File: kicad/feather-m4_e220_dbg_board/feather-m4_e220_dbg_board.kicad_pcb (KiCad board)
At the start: 2 copper layers, 61 x 60.5 mm, 10 parts

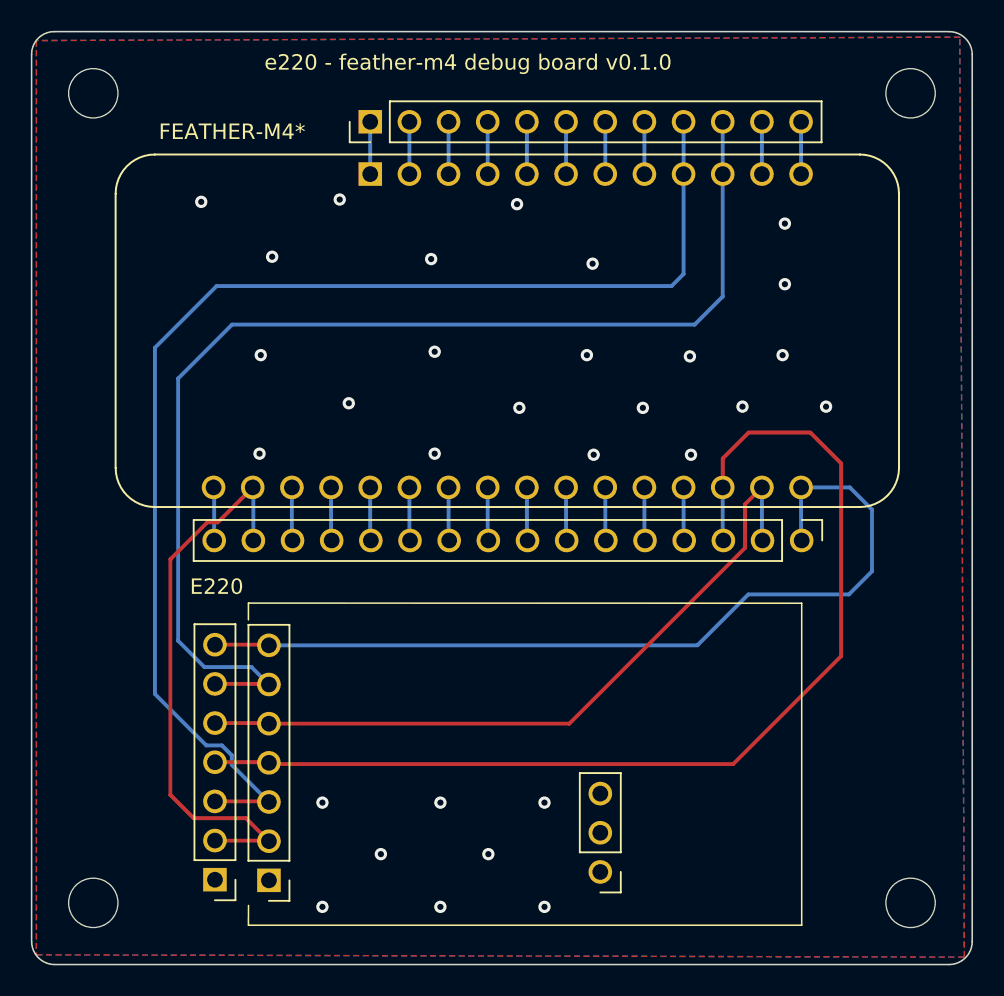
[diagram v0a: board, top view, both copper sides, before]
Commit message: Changed to place through holes for remaining E220 (as Pin8-9)
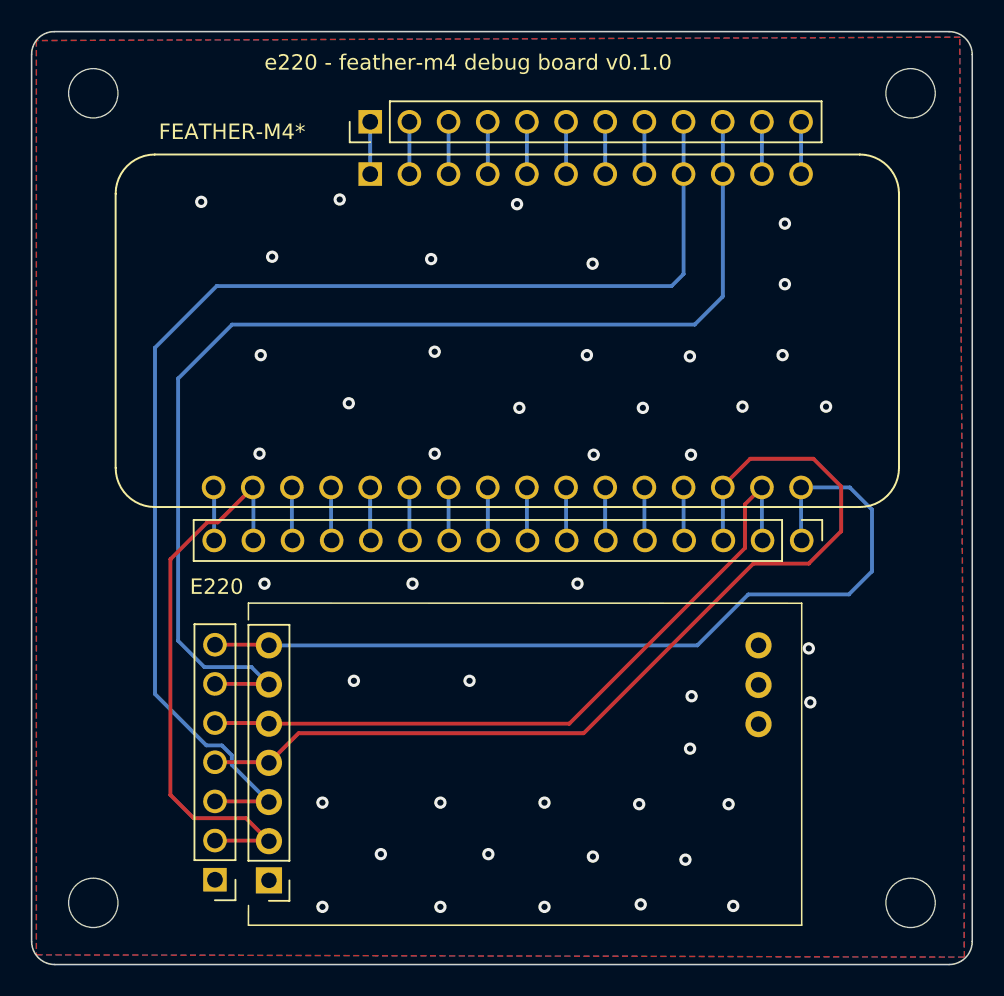
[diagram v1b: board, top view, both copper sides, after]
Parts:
- removed the REF** at (155.9, 124.0)
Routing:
- net Net-(U1-D0): track 70.6 -> 62.4 mm
- net GND: vias 30 -> 45

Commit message: add pin numbers of E220 to PCB
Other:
- board text added: "M0 01 M1 02 RXD 03 TXD 04 AUX 05 VCC 06 GND 07"
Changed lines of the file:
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@@
   (gr_arc (start 120.5 130) (mid 119.43934 129.56066) (end 119 128.5)
     (stroke (width 0.1) (type default)) (layer "Edge.Cuts"))
+  (gr_text "M0 01\nM1 02\nRXD 03\nTXD 04\nAUX 05\nVCC 06\nGND 07" (at 129.5 125.7) (layer "F.SilkS")
+    (effects (font (size 1.59 0.9) (thickness 0.15)) (justify right bottom))
+  )
   (gr_text "e220 - feather-m4 debug board v0.1.0" (at 134.09 72.09) (layer "F.SilkS")
     (effects (font (size 1 1) (thickness 0.15)) (justify left bottom))
